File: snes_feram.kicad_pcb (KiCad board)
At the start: 2 copper layers, 98.5 x 79.5 mm, 34 parts, among them CON1 SNES-EDGE, J1 Conn_01x23_Male, J2 Conn_01x23_Male, SW1 SW_DIP_x04, U1 4081, U2 4071, U3 27C322, U5 74LS245, U6 74LS245, U7 74LS139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

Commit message: Parts annotated
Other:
- board text added: "27C322"
- board text added: "4071"
- board text added: "4081"
- board text added: "74HC139"
- board text added: "74HC245"
- board text added: "FM1808"
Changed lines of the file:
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@@
   (general
     (thickness 1.6)
-    (drawings 41)
+    (drawings 48)
     (tracks 1909)
     (zones 0)
@@
     (tags "SOIC SO")
     (attr smd)
-    (fp_text reference U8 (at 0 0 180) (layer F.SilkS)
+    (fp_text reference U8 (at 0 -9.906 270) (layer F.SilkS)
       (effects (font (size 1 1) (thickness 0.15)))
     )
@@
     (tags "SOIC SO")
     (attr smd)
-    (fp_text reference U7 (at 0 0 180) (layer F.SilkS)
+    (fp_text reference U7 (at 0 5.969 270) (layer F.SilkS)
       (effects (font (size 1 1) (thickness 0.15)))
     )
@@
     (descr "42-lead though-hole mounted DIP package, row spacing 15.24 mm (600 mils)")
     (tags "THT DIP DIL PDIP 2.54mm 15.24mm 600mil")
-    (fp_text reference U3 (at 7.62 25.4 180) (layer F.SilkS)
+    (fp_text reference U3 (at 7.62 -2.286 270) (layer F.SilkS)
       (effects (font (size 1 1) (thickness 0.15)))
     )
@@
     (tags "SOIC SO")
     (attr smd)
-    (fp_text reference U2 (at 0 0 180) (layer F.SilkS)
+    (fp_text reference U2 (at 0 5.334 270) (layer F.SilkS)
       (effects (font (size 1 1) (thickness 0.15)))
     )
@@
     (tags "SOIC SO")
     (attr smd)
-    (fp_text reference U1 (at -0.127 0 180) (layer F.SilkS)
+    (fp_text reference U1 (at 0 5.334 270) (layer F.SilkS)
       (effects (font (size 1 1) (thickness 0.15)))
     )
@@
     )
   )
+  (gr_text 74HC139 (at 151.638 45.339) (layer F.SilkS)
+    (effects (font (size 1 1) (thickness 0.15)))
+  )
+  (gr_text "4071\n" (at 138.557 45.339) (layer F.SilkS)
+    (effects (font (size 1 1) (thickness 0.15)))
+  )
+  (gr_text "4081\n" (at 126.619 45.339) (layer F.SilkS)
+    (effects (font (size 1 1) (thickness 0.15)))
+  )
+  (gr_text FM1808 (at 107.696 50.038) (layer F.SilkS)
+    (effects (font (size 1 1) (thickness 0.15)))
+  )
+  (gr_text "27C322\n" (at 125.349 68.707) (layer F.SilkS)
+    (effects (font (size 1 1) (thickness 0.15)))
+  )
+  (gr_text 74HC245 (at 163.83 84.836) (layer B.SilkS)
+    (effects (font (size 1 1) (thickness 0.15)) (justify mirror))
+  )
+  (gr_text 74HC245 (at 149.098 84.836) (layer B.SilkS)
+    (effects (font (size 1 1) (thickness 0.15)) (justify mirror))
+  )
   (gr_text + (at 169.291 59.309) (layer F.SilkS)

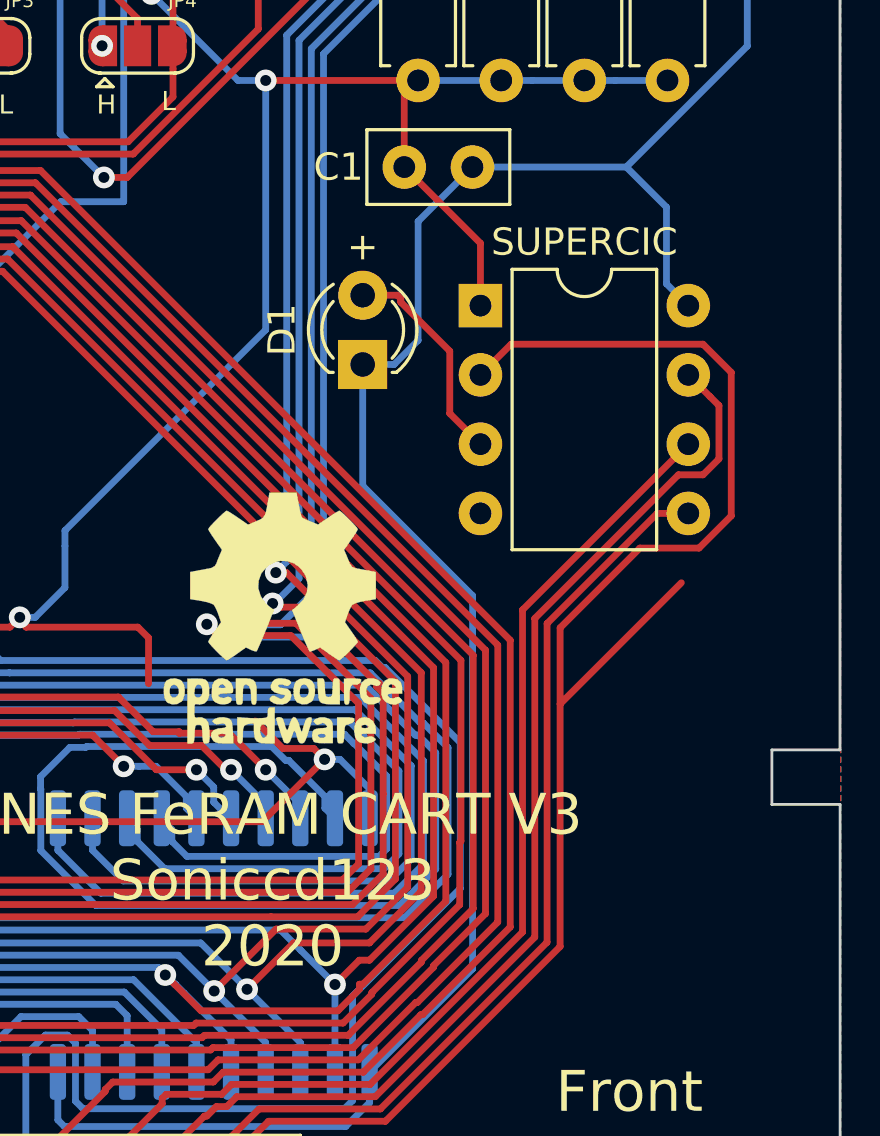
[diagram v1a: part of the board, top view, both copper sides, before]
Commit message: Forgot to add protection resistor to LED
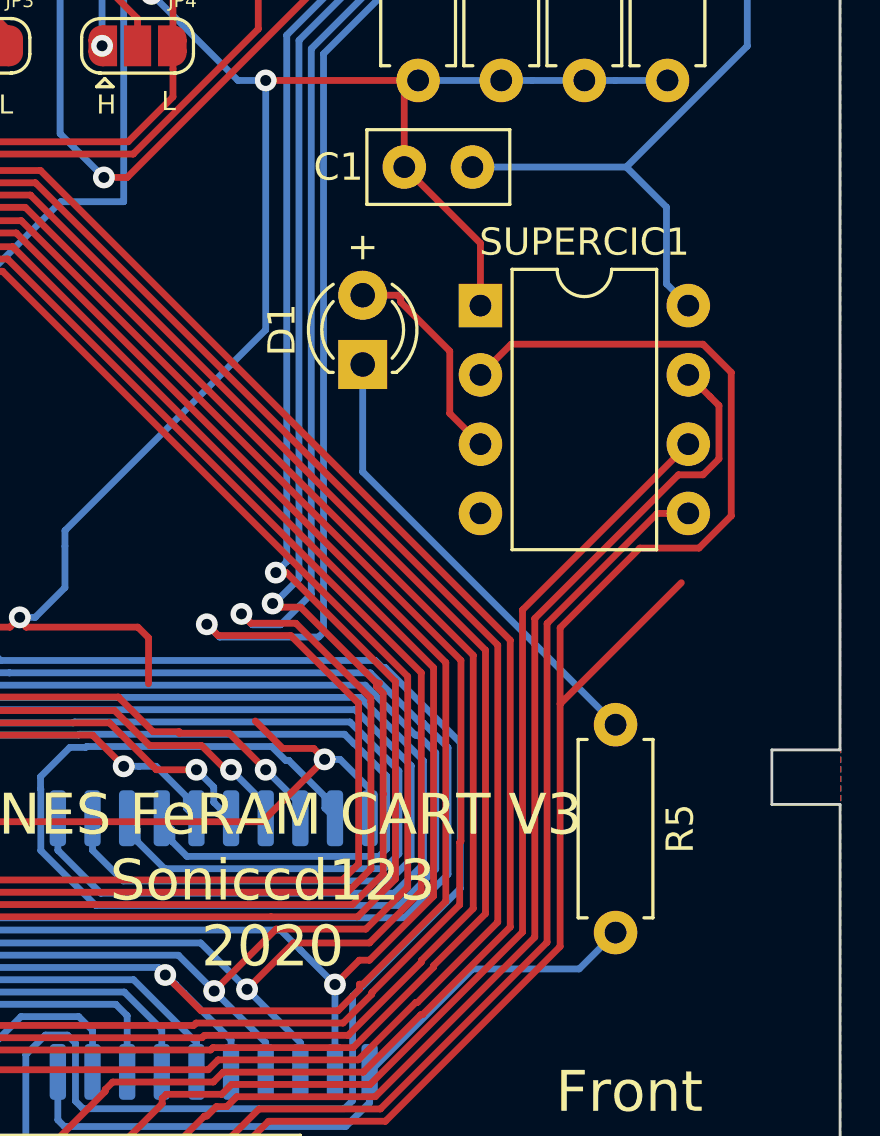
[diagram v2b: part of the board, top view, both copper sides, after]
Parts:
- removed G***: LOGO, OPEN:open_hardware
- added R5: 1K, Resistor_THT:R_Axial_DIN0207_L6.3mm_D2.5mm_P7.62mm_Horizontal, F.Cu at (178.6, 76.8)
- renumbered SUPERCIC to SUPERCIC1
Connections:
- D1 pad 1: GND -> Net-(D1-Pad1)
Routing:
- net GND: track 383.8 -> 356.2 mm
- net Net-(D1-Pad1): track 0.00 -> 17.0 mm

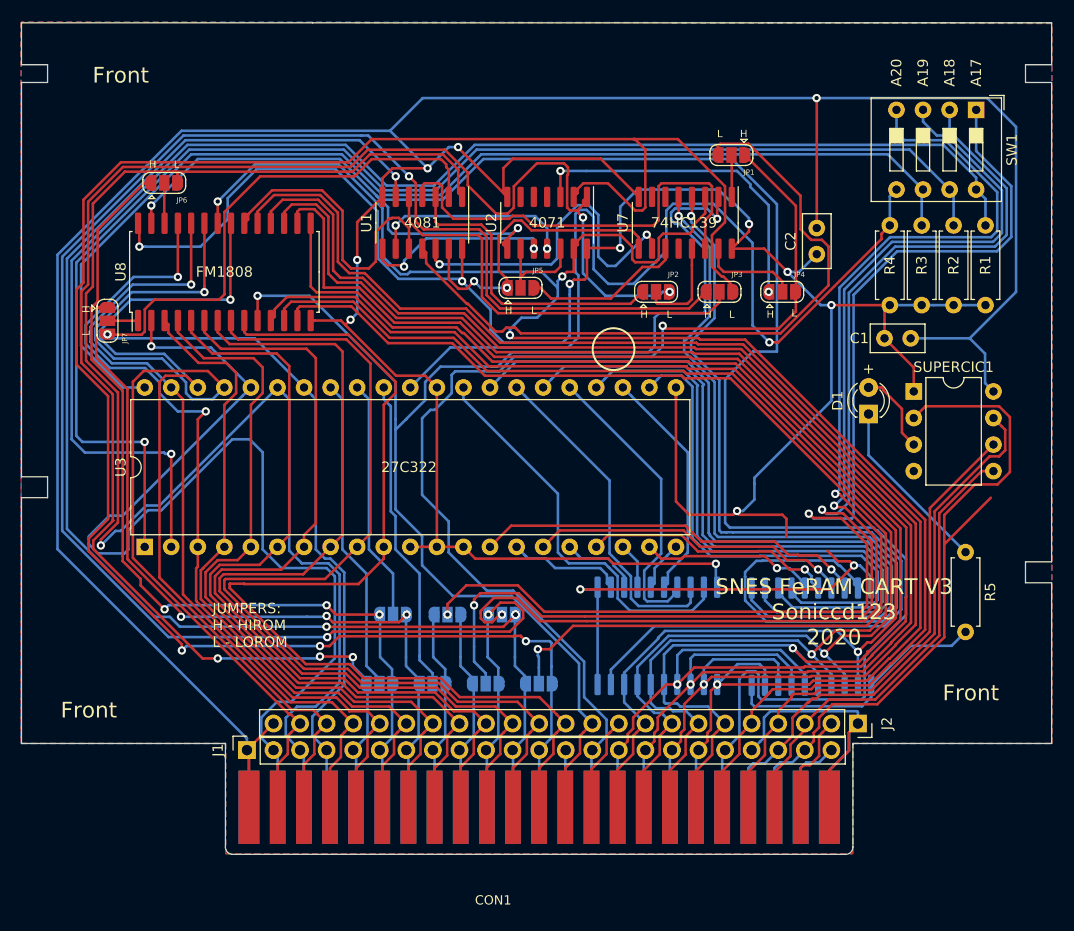
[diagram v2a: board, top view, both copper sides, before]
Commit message: EPROM is now on the back of PCB for better shell fit; Silkscreen mark for shell contact points corrected
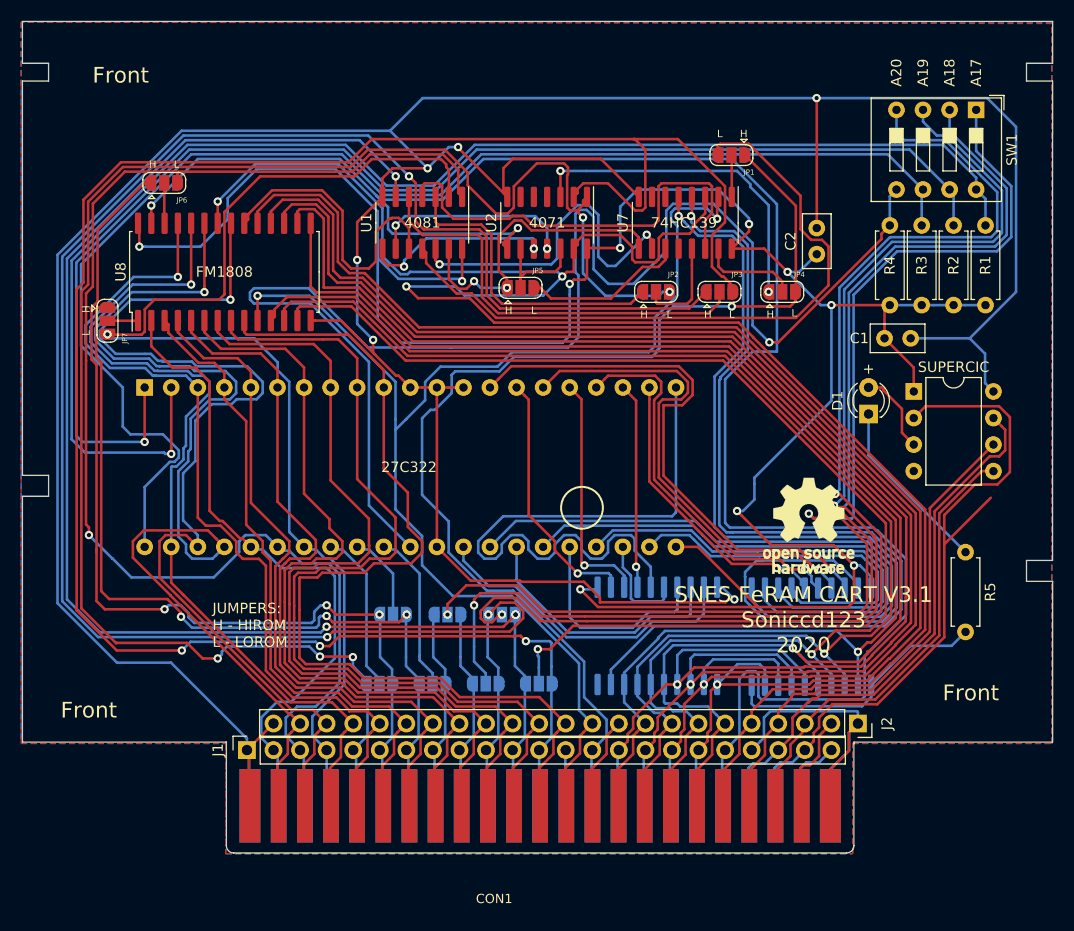
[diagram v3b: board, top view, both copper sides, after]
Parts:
- added G***: LOGO, OPEN:open_hardware, F.Cu at (163.6, 74.3)
- U3: moved to B.Cu
- moved U3 15.2 mm to (100.1, 61.1), turned to 270 degrees
- moved CON1 0.16 mm to (132.6, 114.8)
- renumbered SUPERCIC1 to SUPERCIC
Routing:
- net /D11: track 4.86 -> 60.8 mm
- net /A20_ROM: track 90.2 -> 140.5 mm
- net /A11: track 102.6 -> 62.9 mm, vias 1 -> 0
- net /RD: track 163.7 -> 183.6 mm
- net /A19_ROM: track 108.5 -> 127.3 mm
- net /A12: track 147.6 -> 129.3 mm
- net /D1: track 30.8 -> 47.4 mm
- net /D0: track 37.5 -> 54.2 mm
- net /D9: track 7.50 -> 24.0 mm, vias 0 -> 1
- net /D10: track 4.44 -> 19.7 mm, vias 0 -> 1
- net /D6: track 67.3 -> 52.4 mm
- net /D5: track 58.7 -> 43.8 mm
- net /D4: track 50.4 -> 35.6 mm
- net /D7: track 75.4 -> 60.6 mm
- net /A16: track 30.4 -> 15.7 mm
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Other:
- board text added: "SNES FeRAM CART V3.1 Soniccd123 2020"
- board text removed: "SNES FeRAM CART V3 Soniccd123 2020"
